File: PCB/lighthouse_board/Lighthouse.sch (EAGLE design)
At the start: 15 parts, among them U1 A4988_STEPPER_MOTOR_DRIVER_CA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

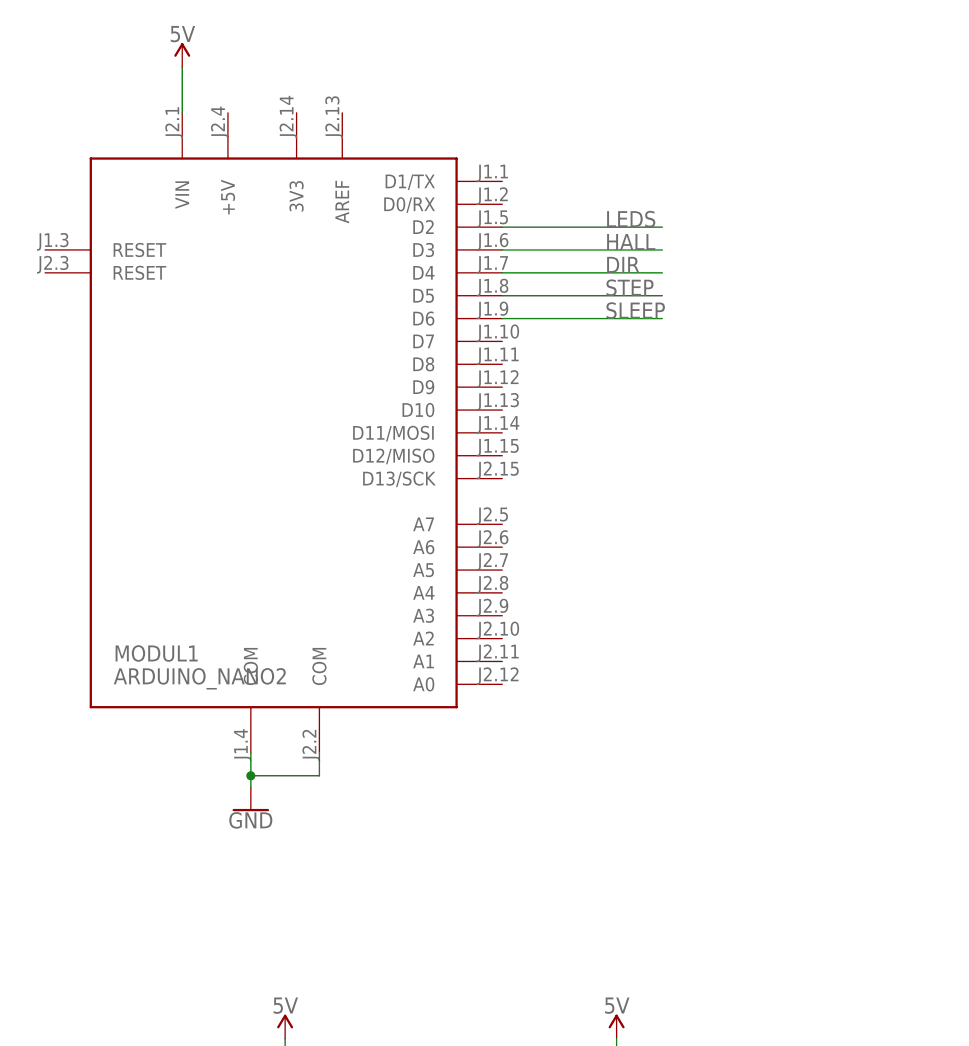
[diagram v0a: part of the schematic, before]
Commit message: new version of stepper pcb and lighthouse pcb
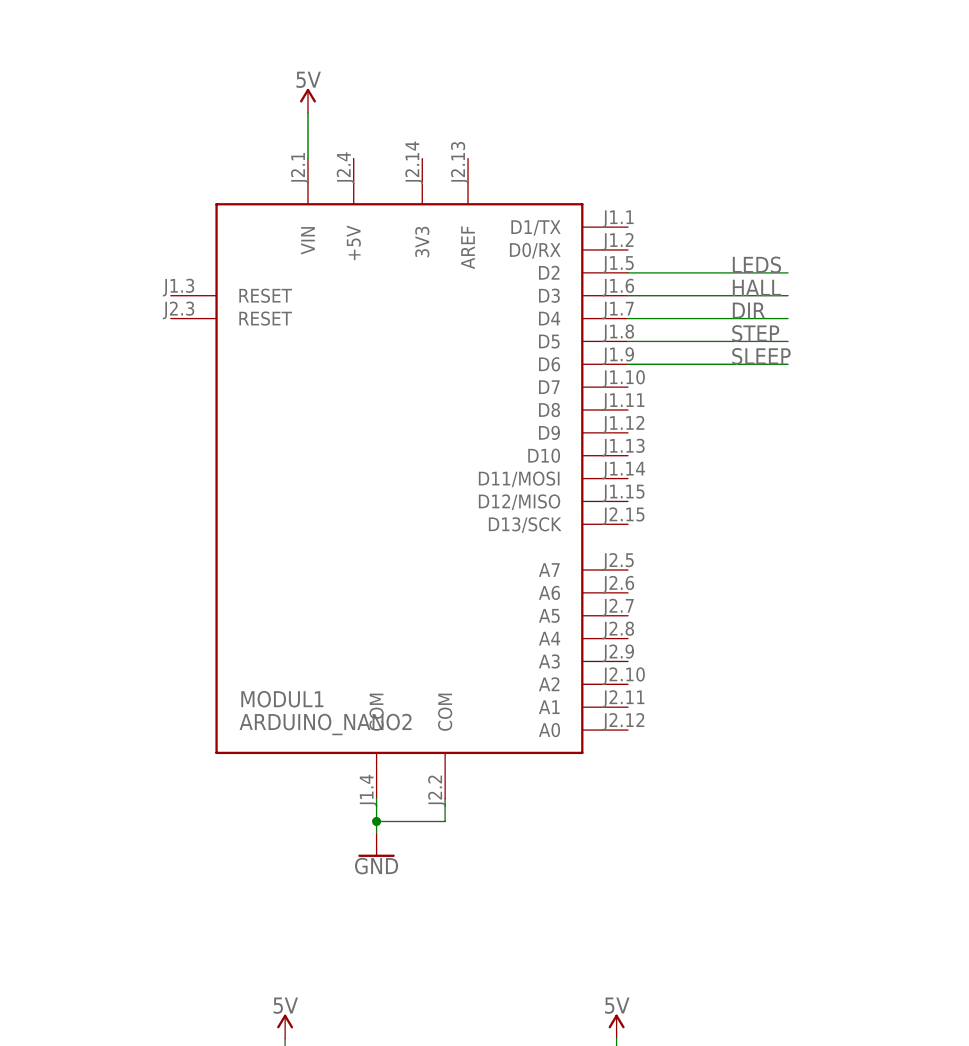
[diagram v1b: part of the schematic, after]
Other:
- moved on the sheet: MODUL1
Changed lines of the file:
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@@
 </plain>
 <instances>
-<instance part="MODUL1" gate="MODUL" x="-144.78" y="81.28" smashed="yes">
-<attribute name="NAME" x="-162.56" y="55.88" size="1.778" layer="95"/>
-<attribute name="VALUE" x="-162.56" y="53.34" size="1.778" layer="96"/>
+<instance part="MODUL1" gate="MODUL" x="-130.81" y="76.2" smashed="yes">
+<attribute name="NAME" x="-148.59" y="50.8" size="1.778" layer="95"/>
+<attribute name="VALUE" x="-148.59" y="48.26" size="1.778" layer="96"/>
 </instance>
 <instance part="J1" gate="G$1" x="-10.16" y="33.02" smashed="yes" rot="R180">
@@
 <attribute name="VALUE" x="-106.68" y="-4.064" size="1.778" layer="96" align="top-center"/>
 </instance>
-<instance part="GND7" gate="1" x="-147.32" y="39.37" smashed="yes">
-<attribute name="VALUE" x="-147.32" y="39.116" size="1.778" layer="96" align="top-center"/>
-</instance>
-<instance part="SUPPLY8" gate="G$1" x="-154.94" y="121.92" smashed="yes">
-<attribute name="VALUE" x="-154.94" y="124.714" size="1.778" layer="96" align="bottom-center"/>
+<instance part="GND7" gate="1" x="-133.35" y="34.29" smashed="yes">
+<attribute name="VALUE" x="-133.35" y="34.036" size="1.778" layer="96" align="top-center"/>
+</instance>
+<instance part="SUPPLY8" gate="G$1" x="-140.97" y="116.84" smashed="yes">
+<attribute name="VALUE" x="-140.97" y="119.634" size="1.778" layer="96" align="bottom-center"/>
 </instance>
 <instance part="SUPPLY1" gate="G$1" x="6.35" y="35.56" smashed="yes">
@@
 <pinref part="SUPPLY8" gate="G$1" pin="5V"/>
 <pinref part="MODUL1" gate="MODUL" pin="VIN"/>
-<wire x1="-154.94" y1="121.92" x2="-154.94" y2="116.84" width="0.1524" layer="91"/>
+<wire x1="-140.97" y1="116.84" x2="-140.97" y2="111.76" width="0.1524" layer="91"/>
 </segment>
 <segment>
@@
 <pinref part="MODUL1" gate="MODUL" pin="COM"/>
 <pinref part="GND7" gate="1" pin="GND"/>
-<wire x1="-147.32" y1="45.72" x2="-147.32" y2="43.18" width="0.1524" layer="91"/>
+<wire x1="-133.35" y1="40.64" x2="-133.35" y2="38.1" width="0.1524" layer="91"/>
 <pinref part="MODUL1" gate="MODUL" pin="COM@1"/>
-<wire x1="-147.32" y1="43.18" x2="-147.32" y2="41.91" width="0.1524" layer="91"/>
-<wire x1="-139.7" y1="45.72" x2="-139.7" y2="43.18" width="0.1524" layer="91"/>
-<wire x1="-139.7" y1="43.18" x2="-147.32" y2="43.18" width="0.1524" layer="91"/>
-<junction x="-147.32" y="43.18"/>
+<wire x1="-133.35" y1="38.1" x2="-133.35" y2="36.83" width="0.1524" layer="91"/>
+<wire x1="-125.73" y1="40.64" x2="-125.73" y2="38.1" width="0.1524" layer="91"/>
+<wire x1="-125.73" y1="38.1" x2="-133.35" y2="38.1" width="0.1524" layer="91"/>
+<junction x="-133.35" y="38.1"/>
 </segment>
 <segment>
@@
 <segment>
 <pinref part="MODUL1" gate="MODUL" pin="D3"/>
-<wire x1="-119.38" y1="101.6" x2="-101.6" y2="101.6" width="0.1524" layer="91"/>
-<label x="-107.95" y="101.6" size="1.778" layer="95"/>
+<wire x1="-105.41" y1="96.52" x2="-87.63" y2="96.52" width="0.1524" layer="91"/>
+<label x="-93.98" y="96.52" size="1.778" layer="95"/>
 </segment>
 </net>
@@
 <segment>
 <pinref part="MODUL1" gate="MODUL" pin="D4"/>
-<wire x1="-119.38" y1="99.06" x2="-101.6" y2="99.06" width="0.1524" layer="91"/>
-<label x="-107.95" y="99.06" size="1.778" layer="95"/>
+<wire x1="-105.41" y1="93.98" x2="-87.63" y2="93.98" width="0.1524" layer="91"/>
+<label x="-93.98" y="93.98" size="1.778" layer="95"/>
 </segment>
 </net>
@@
 <segment>
 <pinref part="MODUL1" gate="MODUL" pin="D5"/>
-<wire x1="-119.38" y1="96.52" x2="-101.6" y2="96.52" width="0.1524" layer="91"/>
-<label x="-107.95" y="96.52" size="1.778" layer="95"/>
+<wire x1="-105.41" y1="91.44" x2="-87.63" y2="91.44" width="0.1524" layer="91"/>
+<label x="-93.98" y="91.44" size="1.778" layer="95"/>
 </segment>
 </net>
@@
 <segment>
 <pinref part="MODUL1" gate="MODUL" pin="D6"/>
-<wire x1="-119.38" y1="93.98" x2="-101.6" y2="93.98" width="0.1524" layer="91"/>
-<label x="-107.95" y="93.98" size="1.778" layer="95"/>
+<wire x1="-105.41" y1="88.9" x2="-87.63" y2="88.9" width="0.1524" layer="91"/>
+<label x="-93.98" y="88.9" size="1.778" layer="95"/>
 </segment>
 </net>
@@
 <segment>
 <pinref part="MODUL1" gate="MODUL" pin="D2"/>
-<wire x1="-119.38" y1="104.14" x2="-101.6" y2="104.14" width="0.1524" layer="91"/>
-<label x="-107.95" y="104.14" size="1.778" layer="95"/>
-</segment>
-</net>
+<wire x1="-105.41" y1="99.06" x2="-87.63" y2="99.06" width="0.1524" layer="91"/>
+<label x="-93.98" y="99.06" size="1.778" layer="95"/>
+</segment>
+</net>

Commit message: update pcb for order
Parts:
- removed J2: (no value), SparkFun-Connectors:CONN_02SCREWTERMINAL-6.35MM-2
- removed J6: (no value), SparkFun-Connectors:CONN_04JST-PTH-VERT
- added J5, J7: (no value), SparkFun-Connectors:CONN_025MM
- J1: value (none) -> B4B-XH-A(LF)(SN); device SparkFun-Connectors:CONN_02SCREWTERMINAL-6.35MM-2 -> B4B-XH-A_LF__SN_:B4B-XH-A(LF)(SN)
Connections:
- net 12V: now also J7.2; no longer J2.1
- net 5V: now also J5.2; no longer J1.1
- net GND: now also J5.1, J7.1; no longer J1.2, J2.2
- net N$10: now also J1.2; no longer J6.3
- net N$7: now also J1.4; no longer J6.1
- net N$8: now also J1.3; no longer J6.2
- net N$9: now also J1.1; no longer J6.4
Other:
- moved on the sheet: +5V, R3
